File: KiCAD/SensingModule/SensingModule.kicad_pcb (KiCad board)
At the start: 2 copper layers, 90 x 70 mm, 44 parts, among them J1 BUS, J2 MONITOR, J3 TERMISTOR, U1 ARDUINO_MKR_WAN_1310, U2 M78AR03305, U3 MCP2562-E-P, U4 MCP2515-I/P, U9 BNO055, Y1 8MHz

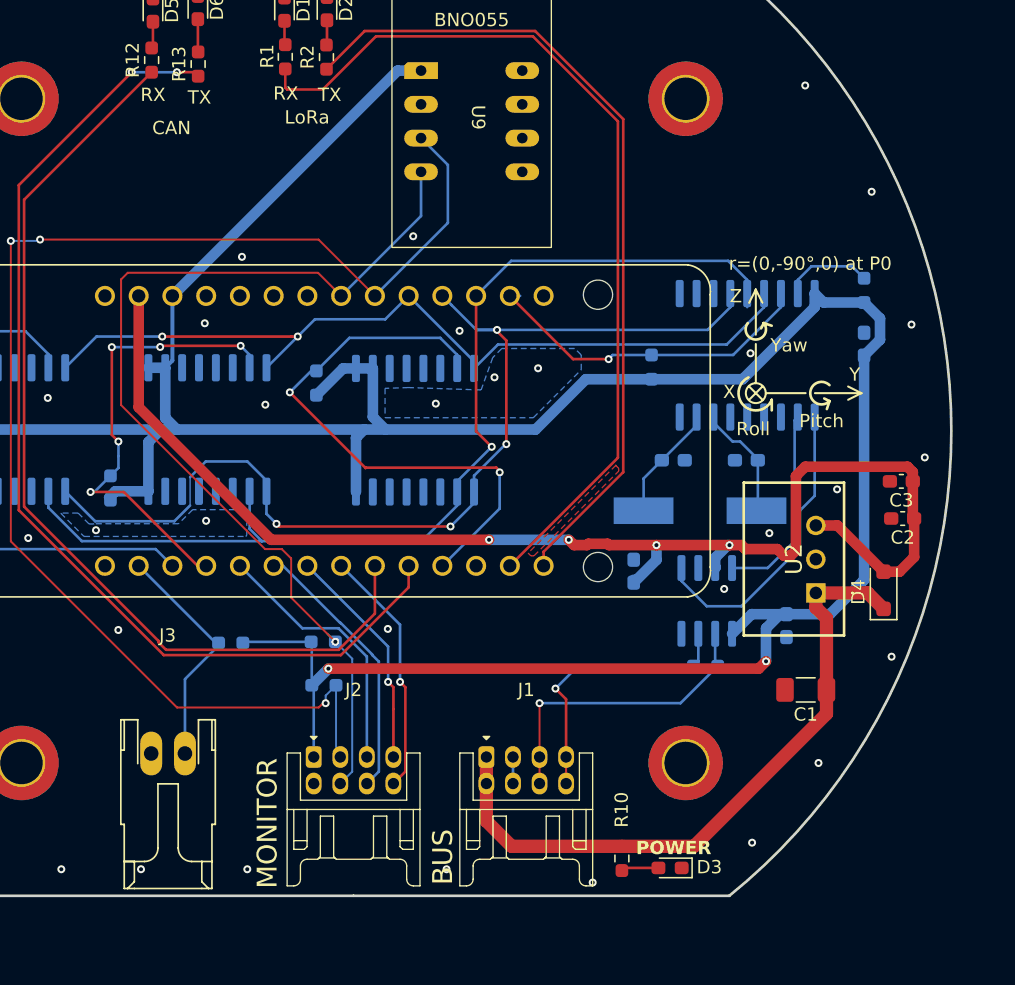
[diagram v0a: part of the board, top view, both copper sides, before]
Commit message: 電源部に保護を追加．DRCエラー無し．
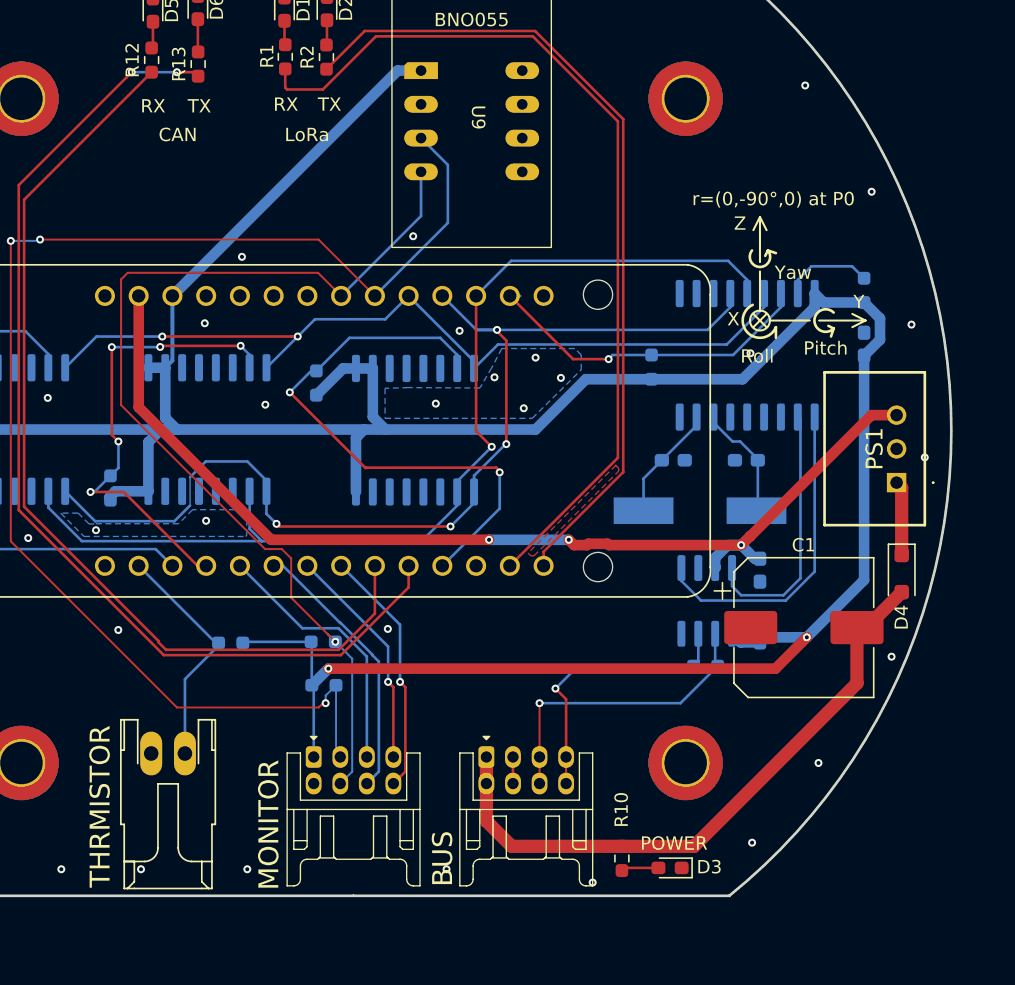
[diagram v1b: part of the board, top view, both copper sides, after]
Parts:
- removed C2: 2.2uF, Capacitor_SMD:C_0603_1608Metric_Pad1.08x0.95mm_HandSolder
- removed C3: 0.1uF, Capacitor_SMD:C_0603_1608Metric_Pad1.08x0.95mm_HandSolder
- removed U2: M78AR03305, TSRP_IC:M78AR03305
- added PS1: M78AR05-0.5, TSRP_IC:M78AR03305, F.Cu at (190.9, 103.9)
- C1: value 10uF -> 330uF; footprint Capacitor_SMD:C_1206_3216Metric_Pad1.33x1.80mm_HandSolder -> Capacitor_SMD:CP_Elec_10x10
- D3: value Greeen -> Green
- moved C4 9.51 mm to (180.6, 110.5), turned to 90 degrees
- moved C1 4.69 mm to (183.9, 114.8), turned to 0 degrees
- moved C5 2.03 mm to (180.6, 115.1), turned to -90 degrees
- moved D4 1.85 mm to (191.3, 110.7), turned to -90 degrees
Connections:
- C1 pad 1: +12V -> GND
- C1 pad 2: GND -> +12V
- D4 pad 1: +12V -> Net-(D4-K)
- D4 pad 2: +5V -> +12V
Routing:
- net +5V: track 99.4 -> 78.9 mm, vias 4 -> 3
- net OSC2: track 18.6 -> 8.67 mm
- net Net-(D4-K): track 0.00 -> 5.61 mm
- net CAN_RX: track 15.0 -> 19.5 mm
- net +12V: track 50.4 -> 47.3 mm
- net CAN_TX: track 22.8 -> 24.1 mm
- net SPI_MOSI: track 80.2 -> 79.2 mm
- net GND: vias 48 -> 47
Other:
- board text added: "THRMISTOR"

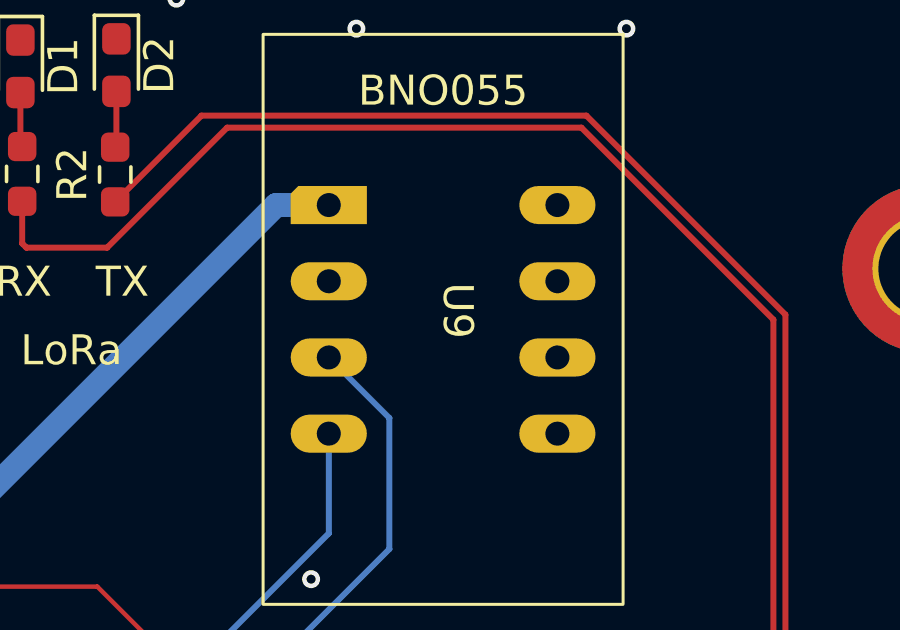
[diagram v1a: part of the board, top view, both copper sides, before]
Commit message: BNO055のシンボルを変更．
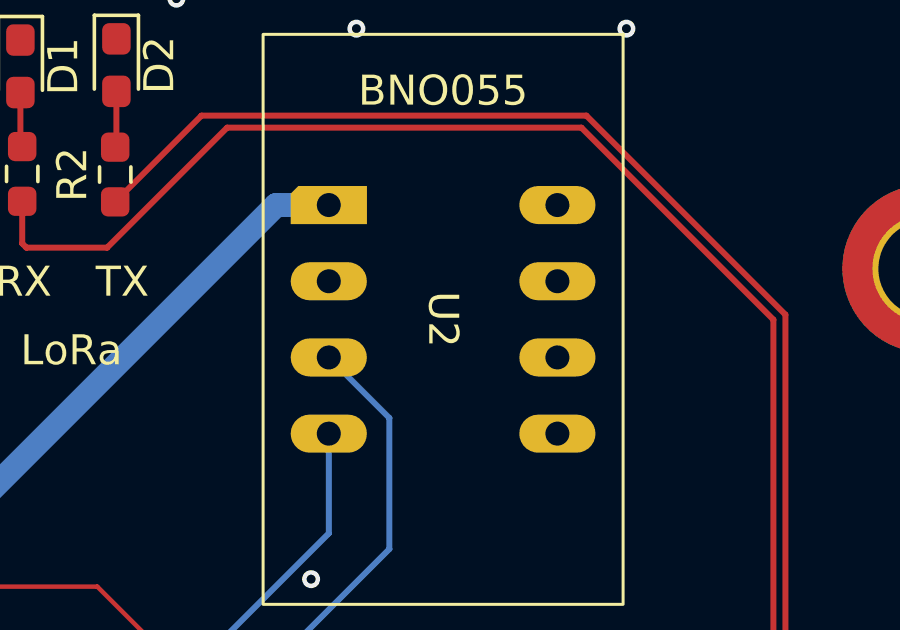
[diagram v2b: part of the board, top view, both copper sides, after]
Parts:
- removed U9: BNO055, TSRP_IC:AE-BNO055-BO
- added U2: ~, TSRP_IC:AE-BNO055-BO, F.Cu at (158.9, 76.7)

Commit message: Sensing Build-1完成
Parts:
- added G***: LOGO, LOGO, B.Cu at (136.9, 131.4)
- added G***: LOGO, LOGO, B.Cu at (162.9, 130.8)
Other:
- board text added: "DCDC"
- board text added: "SUBARU"
- board text added: "Sensing Module Build-1"
- board text added: "Tokai Student Rocket Project"
- board text added: "V1.3"

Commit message: 最終確認終わり
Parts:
- moved D3 4.19 mm to (169.7, 132.3), turned to 90 degrees
- moved R10 1.51 mm to (171.7, 132.3)
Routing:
- net CAN_H: track 21.1 -> 19.5 mm
- net +12V: track 47.3 -> 48.2 mm
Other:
- board text added: "12V"
- board text removed: "POWER"

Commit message: 取り付け穴位置を更新
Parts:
- moved H5 5.83 mm to (120.0, 72.0)
- moved H6 5.83 mm to (120.0, 128.0)
- moved H7 5.83 mm to (180.0, 128.0)
- moved H8 5.83 mm to (180.0, 72.0)
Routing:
- net +12V: track 48.2 -> 47.1 mm

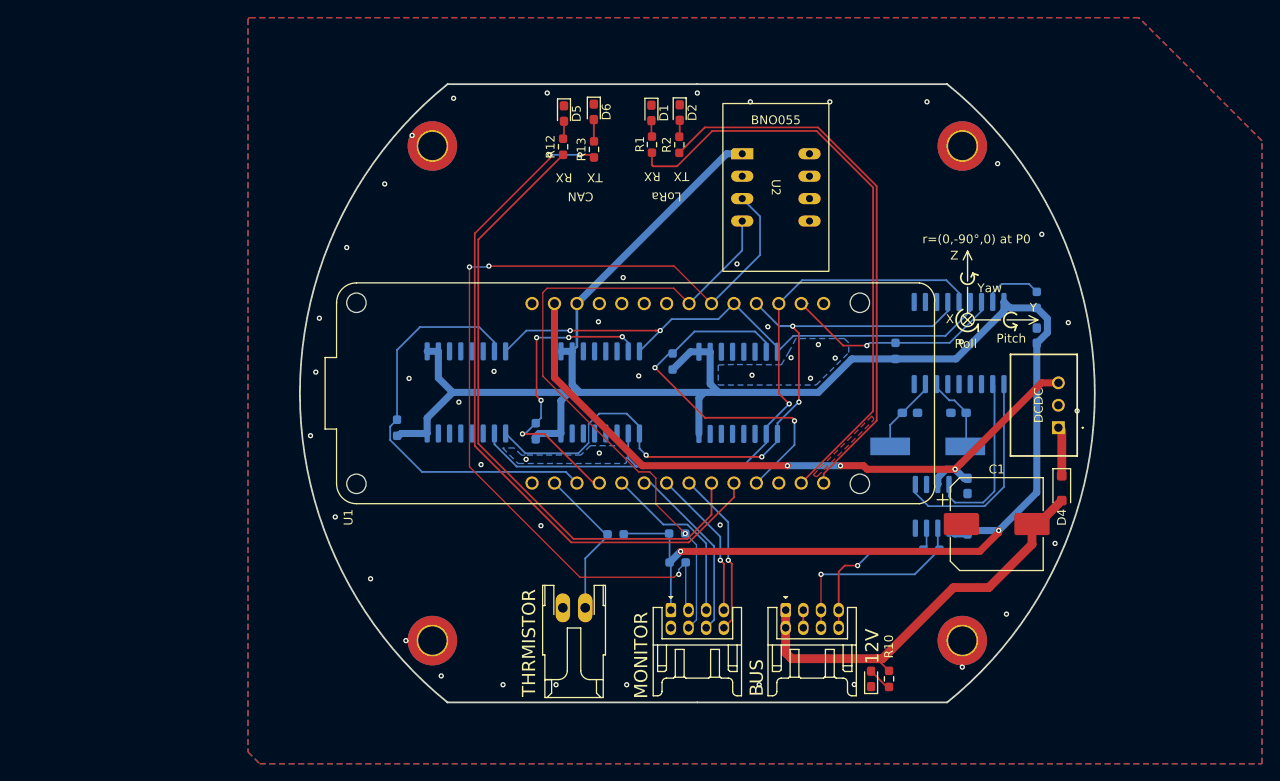
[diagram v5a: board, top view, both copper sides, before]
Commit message: 3Dモデルを組み合わせて結合試験する
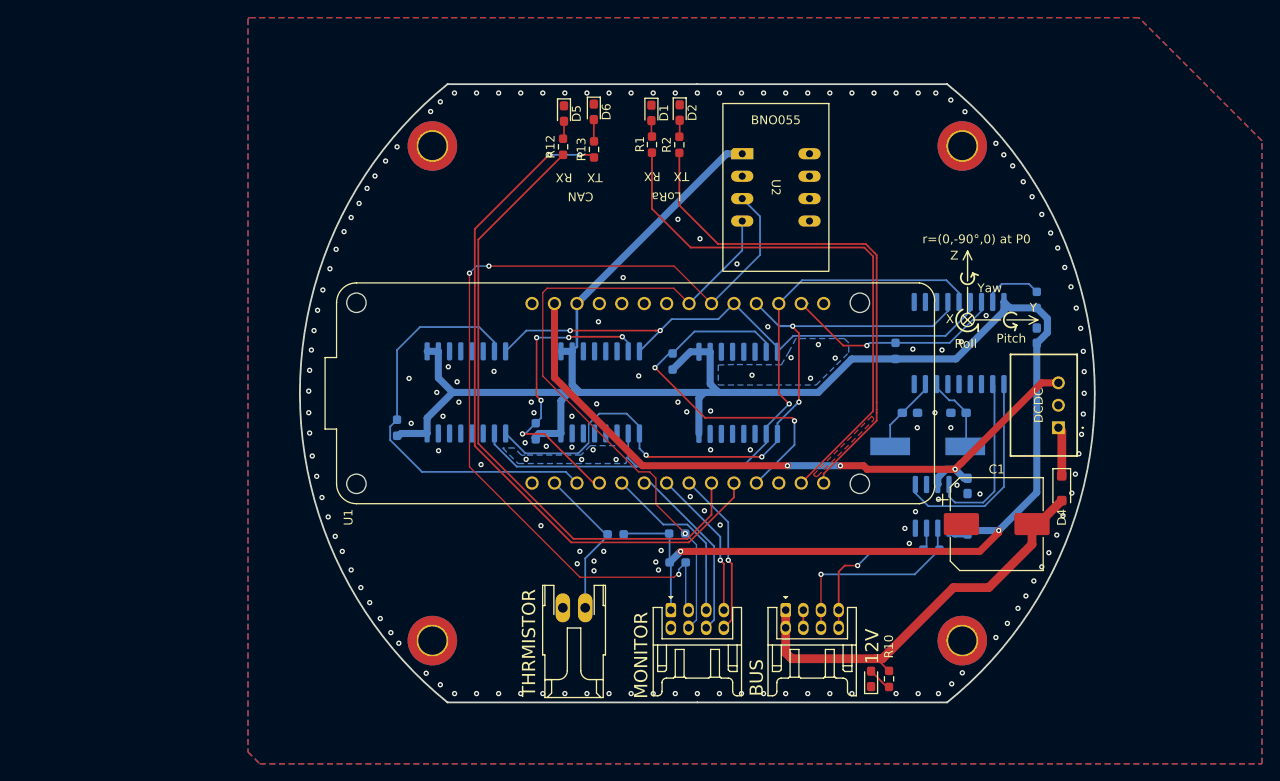
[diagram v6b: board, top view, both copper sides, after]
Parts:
- removed the G*** at (136.9, 131.4)
- removed the G*** at (162.9, 130.8)
- added G***: LOGO, LOGO, B.Cu at (164.9, 131.3)
- added G***: LOGO, LOGO, B.Cu at (135.5, 131.3)
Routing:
- net LORA_RECEIVE_STATUS: track 67.6 -> 62.7 mm
- net LORA_SEND_STATUS: track 62.4 -> 58.9 mm
- net GND: vias 47 -> 174

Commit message: 最終確認終わり
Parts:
- J3: value TERMISTOR -> DF51-2P-2DS; footprint TSRP_Connector_Hirose:DF1B-2S-2.5R -> TSRP_Connector_Hirose:DF51-2P-2DS
- moved J3 9.63 mm to (135.3, 134.6)
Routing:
- net VREF_THERMISTOR: track 17.8 -> 19.1 mm

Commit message: きれいに配線できるようになった．
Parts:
- removed D4: GS1010FL, Diode_SMD:D_SOD-123F
- removed J2: MONITOR, TSRP_Connector_Hirose:DF11-8DP-2DS
- removed R16: 4.7kR, Resistor_SMD:R_0603_1608Metric_Pad0.98x0.95mm_HandSolder
- removed U12, U13, U14: ~, Package_SO:SOIC-16W_7.5x10.3mm_P1.27mm
- added C10: 1uF, Capacitor_SMD:C_0805_2012Metric_Pad1.18x1.45mm_HandSolder, B.Cu at (189.0, 86.9)
- added C11: 1uF, Capacitor_SMD:C_0805_2012Metric_Pad1.18x1.45mm_HandSolder, B.Cu at (181.4, 86.9)
- added C14: 0.1uF, Capacitor_SMD:C_0603_1608Metric_Pad1.08x0.95mm_HandSolder, B.Cu at (117.1, 96.3)
- added C15: 0.1uF, Capacitor_SMD:C_0603_1608Metric_Pad1.08x0.95mm_HandSolder, B.Cu at (145.3, 103.1)
- added C16: 0.1uF, Capacitor_SMD:C_0603_1608Metric_Pad1.08x0.95mm_HandSolder, B.Cu at (147.8, 96.3)
- added C17: 0.1uF, Capacitor_SMD:C_0603_1608Metric_Pad1.08x0.95mm_HandSolder, F.Cu at (147.6, 70.9)
- added D7: SB34AFC, Diode_SMD:D_SMA_Handsoldering, F.Cu at (188.0, 107.4)
- added J4: DF51A-4P-2DS, TSRP_Connector_Hirose:DF51A-4P-2DS, F.Cu at (138.4, 65.9)
- added R17: 4.7kR, Resistor_SMD:R_0603_1608Metric_Pad0.98x0.95mm_HandSolder, B.Cu at (161.0, 96.3)
- added U5: MB85RQ8MX, Package_SO:SOIC-16W_7.5x10.3mm_P1.27mm, B.Cu at (123.8, 100.0)
- added U6: MB85RQ8MX, Package_SO:SOIC-16W_7.5x10.3mm_P1.27mm, B.Cu at (138.8, 100.0)
- added U7: MB85RQ8MX, Package_SO:SOIC-16W_7.5x10.3mm_P1.27mm, B.Cu at (154.4, 100.0)
- added U8: NCV8114BSN330T1G, Package_TO_SOT_SMD:TSOT-23-5, B.Cu at (184.9, 88.9)
- R7, R8: moved to F.Cu
- U4: footprint Package_SO:SOIC-18W_7.5x11.6mm_P1.27mm -> Package_SO:TSSOP-20_4.4x6.5mm_P0.65mm
- moved D1 78.3 mm to (75.4, 104.5)
- moved R1 78.3 mm to (75.4, 108.1)
- moved R2 78.3 mm to (78.5, 108.1)
- moved D2 78.3 mm to (78.6, 104.5)
- moved D6 70.2 mm to (89.1, 118.2), turned to 0 degrees
- moved D5 65.8 mm to (89.1, 115.6), turned to 0 degrees
- moved R13 64.0 mm to (93.5, 118.1), turned to 0 degrees
- moved R12 60.0 mm to (93.5, 115.6), turned to 0 degrees
- moved R7 40.2 mm to (148.6, 79.0), turned to 0 degrees
- moved R8 33.8 mm to (148.3, 82.0), turned to 0 degrees
- moved R6 16.4 mm to (130.6, 96.3), turned to 90 degrees
- moved R11 12.0 mm to (164.8, 120.7), turned to 180 degrees
- moved R14 11.1 mm to (177.3, 89.2), turned to -90 degrees
- moved C6 10.3 mm to (179.1, 89.2)
- moved R10 8.73 mm to (169.7, 123.8)
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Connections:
- net SPI_CS_FRAM1 renamed SPI_~{CS}_FeRAM1
- C5 pad 2: +3.3V -> +3.3VP
- C6 pad 2: +3.3V -> +3.3VP
- H5 pad 1: GND -> (no net)
- H6 pad 1: GND -> (no net)
- H7 pad 1: GND -> (no net)
- H8 pad 1: GND -> (no net)
- R14 pad 1: +3.3V -> +3.3VP
- R6 pad 1: SPI_CS_FRAM0 -> SPI_~{CS}_FeRAM0
- R9 pad 2: +3.3V -> +3.3VP
- U1 pad J3_11: SPI_CS_FRAM2 -> unconnected-(U1-PA10/D2(PWM)-PadJ3_11)
- U1 pad J3_3: SPI_CS_FRAM0 -> unconnected-(U1-PB02/D16/AIN(10)/A1-PadJ3_3)
- U1 pad J5_8: unconnected-(U1-PB23/D13/RX(SC5)-PadJ5_8) -> SPI_~{CS}_FeRAM2
- U1 pad J5_9: unconnected-(U1-PB22/D14/TX(SC5)-PadJ5_9) -> SPI_~{CS}_FeRAM0
- U3 pad 5: +3.3V -> +3.3VP
- U4 pad 18: +3.3V -> +3.3VP
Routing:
- net +3.3V: track 234.5 -> 110.3 mm, vias 2 -> 6
- net I2C_SDA: track 102.6 -> 15.0 mm, vias 3 -> 0
- net CAN_SEND_STATUS: track 79.3 -> 0.00 mm, vias 2 -> 0
- net CAN_RECEIVE_STATUS: track 72.3 -> 0.00 mm
- net I2C_SCK: track 76.5 -> 11.8 mm, vias 1 -> 0
- net LORA_RECEIVE_STATUS: track 62.7 -> 0.00 mm
- net LORA_SEND_STATUS: track 58.9 -> 0.00 mm
- net +3.3VP: track 0.00 -> 52.2 mm
- net SPI_CS_FRAM0: track 47.5 -> 0.00 mm
- net SPI_CS_FRAM2: track 43.1 -> 0.00 mm, vias 2 -> 0
- net SPI_~{CS}_FeRAM1: track 34.8 -> 11.8 mm, vias 5 -> 1
- net SPI_~{CS}_FeRAM0: track 0.00 -> 23.0 mm, vias 0 -> 1
- net SPI_CS_MCP: track 25.8 -> 3.28 mm, vias 1 -> 0
- net SPI_MISO: track 63.7 -> 85.1 mm, vias 2 -> 3
- net VREF_T2: track 20.5 -> 0.00 mm
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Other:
- board text removed: "CAN"
- board text removed: "LoRa"
- board text removed: "MONITOR"
- board text removed: "RX"
- board text removed: "TX"
